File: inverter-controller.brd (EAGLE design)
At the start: 18.5 x 87.2 mm, 114 parts, among them IC1 STM32F334C8T6, IC2 SY7152ABC, IC3 LMV358MMX, IC4 LMV358MMX, J1 621006245821, J2 61300211121, X1 0289-9066**15EDGVC-3.81-02P-14, X2 0289-9066**15EDGVC-3.81-02P-14, X6 1365-16, Y1 NX2016SA-32M

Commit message: RS485 eklendi.
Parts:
- added C49, C50: 1019-3166**CAP 0603 CER 100nF 16V %10 X7R (AbC), rcl:C0603
- added C51, C53: 1019-3168","CAP 0805 CER 2.2uF 16V %10 X7R (AbC), rcl:C0805
- added C52: 0019-3020","CAP TH CER 470pF 3kV Y5P %10 85C F=7.5 D=8.5, rcl:C050-055X075
- added C60, C61: 1200920378**CAP 0603 CER 100p 50V%5 NP0, rcl:C0603
- added C66: NC, rcl:C0603
- added D10: 1119-3034_ESD Protection Diode for CANBUS NXP PESD2CAN SOT23, diode:SOT23
- added IC10: ISO3082, enko:ISO3082
- added L1: 1319-4025","INDUCTOR SMD 0805 4.7uH 500mA CL2012C-4R7M Core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, rcl:R0805
- added L6: 1319-4002_ACM2012 SMD Common Mode Filter, enko:ACM2012-900--2P-T002
- added LED4: 1209-0004**LED GREEN CLEAR THIN 0805 SMD, led:CHIP-LED0805
- added Q17: 1039-2335","DC-DC Converter 5V to 5V 1W RFMM-0505S, enko:RFMM-0505S
- added R41: 1029-2232**RES 0603 120R %1, rcl:R0603
- added R48: 1409-0025**RES 0603 470R %5 1/16W, rcl:R0603
- added R65, R66, R69: 1029-2003**RES 0603 10R %1, rcl:R0603
- added TP11, TP4, TP5, TP6, TP7, TP8: PTR1TP18R, testpad:TP18R
- added X3: 0289-9068**15EDGVC-3.81-03P-14, con-phoenix-381_l:MCV3
- moved X2 12.4 mm to (4.24, 12.8), turned to 90 degrees
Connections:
- new net +5V: C51.1, L1.1
- new net 485A_PORT: D10.1, R41.1, R69.1, X3.2
- new net 485B_PORT: D10.2, R41.2, R66.2, X3.1
- new net 485G_PORT1: C66.1, R65.2, X3.3
- new net N$24: LED4.A, R48.2
- new net N$41: C61.1, IC10.12, L6.2, TP8.TP
- new net N$42: L6.4, R66.1
- new net N$57: L6.3, R69.2
- new net N$73: C60.2, IC10.13, L6.1, TP7.TP
- new net N$80: C52.1, L1.2, Q17.1
- new net RS485_DIR: IC1.39, IC10.4, IC10.5, TP5.TP
- new net RS485_ISO_5V: C50.2, C52.2, C53.1, IC10.16, Q17.7
- new net RS485_ISO_GND: C50.1, C53.2, C60.1, C61.2, C66.2, D10.3, IC10.10, IC10.15, IC10.9, Q17.5, R65.1
- new net RS485_LED: IC1.40, LED4.C, TP11.TP
- new net RS485_RX: IC1.22, IC10.3, TP4.TP
- new net RS485_TX: IC1.21, IC10.6, TP6.TP
- net +3V3: now also C49.2, IC10.1, R48.1
- net GND: now also C49.1, C51.2, IC10.2, IC10.7, IC10.8, Q17.2

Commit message: RS485 DC-DC besleme gerilimi 3V yapildi.
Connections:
- removed net +5V: C51.1, L1.1
- net +3V3: now also C51.1, L1.1
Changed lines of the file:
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@@
 <contactref element="IC10" pad="1"/>
 <contactref element="R48" pad="1"/>
+<contactref element="C51" pad="1"/>
+<contactref element="L1" pad="1"/>
 <wire x1="-132.7238" y1="-366.64" x2="-132.7238" y2="-371.63" width="0" layer="19" extent="1-1"/>
 <wire x1="-132.7238" y1="-376.62" x2="-132.7238" y2="-371.63" width="0" layer="19" extent="1-1"/>
@@
 <wire x1="-27.91" y1="111.76" x2="5.172" y2="58.76" width="0" layer="19" extent="1-16"/>
 <wire x1="-96.445" y1="-593.1" x2="-132.7238" y2="-376.62" width="0" layer="19" extent="1-1"/>
-<wire x1="-144.85" y1="-690.5" x2="-96.445" y2="-593.1" width="0" layer="19" extent="1-1"/>
+<wire x1="-144.55" y1="-671.5" x2="-96.445" y2="-593.1" width="0" layer="19" extent="1-1"/>
+<wire x1="-144.55" y1="-684.5" x2="-144.55" y2="-671.5" width="0" layer="19" extent="1-1"/>
+<wire x1="-144.85" y1="-690.5" x2="-144.55" y2="-684.5" width="0" layer="19" extent="1-1"/>
 <wire x1="-116.15" y1="-701.5" x2="-144.85" y2="-690.5" width="0" layer="19" extent="1-1"/>
 </signal>
@@
 <wire x1="-124.9862" y1="-152.14" x2="-131.81" y2="-166.08" width="0" layer="19" extent="1-1"/>
 </signal>
-<signal name="+5V">
-<contactref element="C51" pad="1"/>
-<contactref element="L1" pad="1"/>
-<wire x1="-144.55" y1="-671.5" x2="-144.55" y2="-684.5" width="0" layer="19" extent="1-1"/>
-</signal>
 <signal name="485G_PORT1">

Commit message: Programlama soketi baglantilari duzeltildi.
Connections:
- net FAN2_EN renamed SWDIO
- removed net RELAY_EN: J1.2
- removed net SPI1_SCK: J1.6
- new net SWCLK: IC1.37, J1.2
- new net SWO: IC1.39, J1.6
- net RS485_DIR: now also IC1.41; no longer IC1.39
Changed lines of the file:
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@@
 <wire x1="-80.54" y1="106.68" x2="-74.19" y2="106.68" width="0" layer="19" extent="1-1"/>
-</signal>
-<signal name="SPI1_SCK">
-<contactref element="J1" pad="6"/>
 </signal>
 <signal name="NRST">
@@
 <wire x1="-131.1362" y1="-430.12" x2="-136.76" y2="-430.53" width="0" layer="19" extent="1-1"/>
 </signal>
-<signal name="FAN2_EN">
-<contactref element="IC1" pad="34"/>
-<contactref element="J1" pad="4"/>
-<wire x1="13.648" y1="55.76" x2="13.83" y2="84.16" width="0" layer="19" extent="1-16"/>
-</signal>
-<signal name="RELAY_EN">
-<contactref element="J1" pad="2"/>
-</signal>
 <signal name="N$35">
 <contactref element="LED8" pad="A"/>
@@
 <contactref element="IC10" pad="5"/>
 <contactref element="TP5" pad="TP"/>
-<contactref element="IC1" pad="39"/>
+<contactref element="IC1" pad="41"/>
 <wire x1="-91.365" y1="-593.1" x2="-92.635" y2="-593.1" width="0" layer="19" extent="1-1"/>
 <wire x1="-79" y1="-718" x2="-91.365" y2="-593.1" width="0" layer="19" extent="1-1"/>
-<wire x1="11.16" y1="53.272" x2="-91.365" y2="-593.1" width="0" layer="19" extent="1-16"/>
+<wire x1="10.16" y1="53.272" x2="-91.365" y2="-593.1" width="0" layer="19" extent="1-16"/>
 </signal>
 <signal name="RS485_TX">
@@
 <wire x1="11.16" y1="61.748" x2="-93.905" y2="-593.1" width="0" layer="19" extent="1-16"/>
 </signal>
+<signal name="SWO">
+<contactref element="IC1" pad="39"/>
+<contactref element="J1" pad="6"/>
+<wire x1="11.16" y1="53.272" x2="15.83" y2="84.16" width="0" layer="19" extent="1-16"/>
+</signal>
+<signal name="SWDIO">
+<contactref element="IC1" pad="34"/>
+<contactref element="J1" pad="4"/>
+<wire x1="13.648" y1="55.76" x2="13.83" y2="84.16" width="0" layer="19" extent="1-16"/>
+</signal>
+<signal name="SWCLK">
+<contactref element="IC1" pad="37"/>
+<contactref element="J1" pad="2"/>
+<wire x1="12.16" y1="53.272" x2="11.83" y2="84.16" width="0" layer="19" extent="1-16"/>
+</signal>
 </signals>

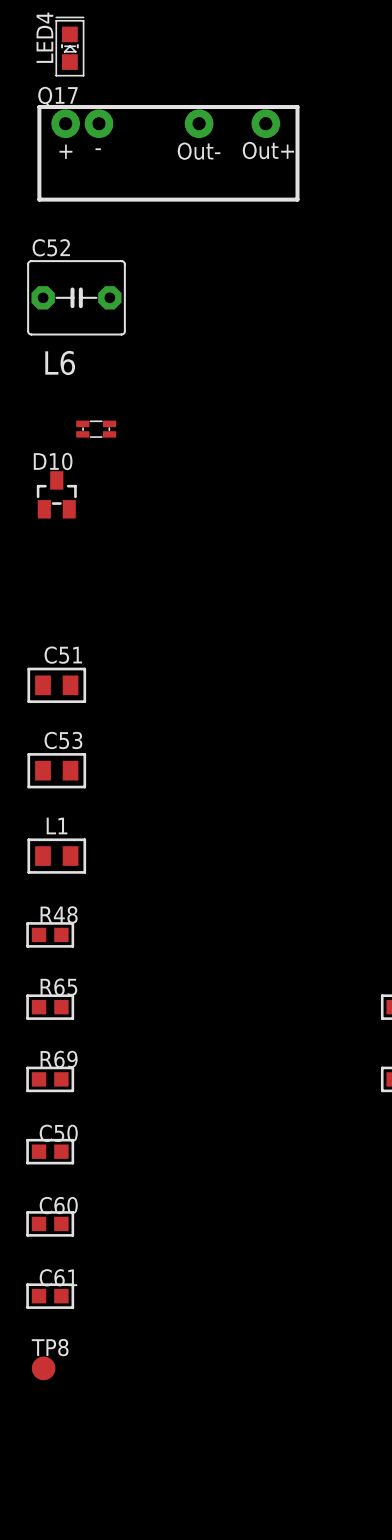
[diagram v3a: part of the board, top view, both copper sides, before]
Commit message: RS485 DC-DC paketi degistirildi.
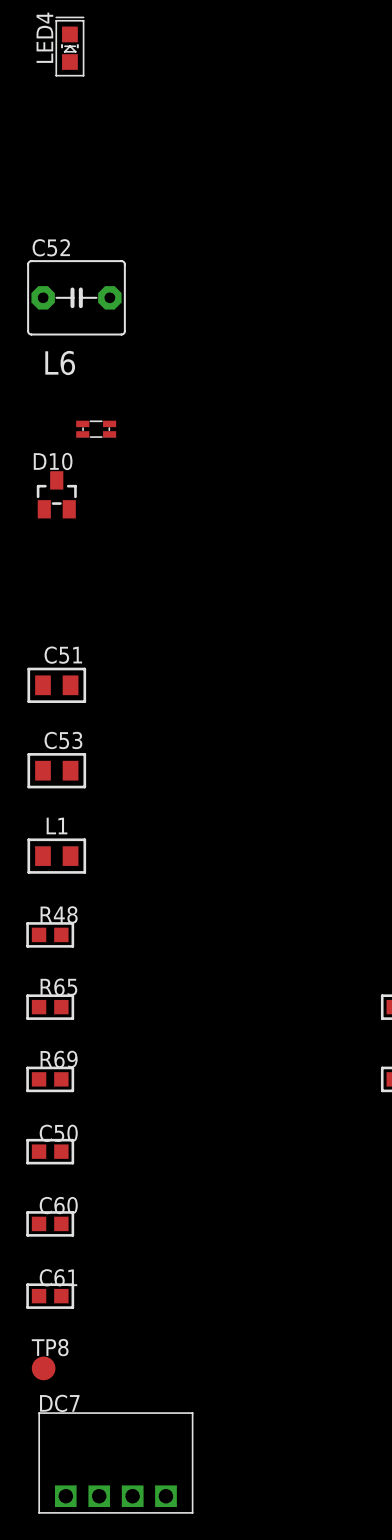
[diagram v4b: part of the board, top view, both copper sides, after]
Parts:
- removed Q17: 1039-2335","DC-DC Converter 5V to 5V 1W RFMM-0505S, enko:RFMM-0505S
- added DC7: RI-0512S/P_DC_DC_5V_12V, my_parts1:RI-0512S/P_DC_DC_5V_12V
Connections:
- removed net RELAY3: IC1.26
- removed net USART1_DIR: IC1.2
- net GND: now also DC7.1-IN; no longer Q17.2
- net N$80: now also DC7.2+IN; no longer Q17.1
- net RS485_ISO_5V: now also DC7.4+VOU; no longer Q17.7
- net RS485_ISO_GND: now also DC7.3-VOUT; no longer Q17.5
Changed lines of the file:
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@@
 <attribute name="VALUE" x="-138.85" y="-594.834" size="1.778" layer="27" ratio="10"/>
-</element>
-<element name="Q17" library="enko" package="RFMM-0505S" value="1039-2335&quot;,&quot;DC-DC Converter 5V to 5V 1W RFMM-0505S" x="-135" y="-631" smashed="yes">
-<attribute name="NAME" x="-145" y="-627.23" size="1.27" layer="25"/>
-<attribute name="VALUE" x="-145.12" y="-636.02" size="1.27" layer="27"/>
 </element>
 <element name="C51" library="rcl" package="C0805" value="1019-3168&quot;,&quot;CAP 0805 CER 2.2uF 16V %10 X7R (AbC)" x="-143.5" y="-671.5" smashed="yes">
@@
 <attribute name="TP_SIGNAL_NAME" value="" x="-89" y="-720.54" size="1" layer="37"/>
 <attribute name="VALUE" x="-89.762" y="-718.889" size="0.0254" layer="27"/>
+</element>
+<element name="DC7" library="my_parts1" package="RI-0512S/P_DC_DC_5V_12V" value="RI-0512S/P_DC_DC_5V_12V" x="-139" y="-734.5" smashed="yes">
+<attribute name="NAME" x="-144.93" y="-726.8" size="1.27" layer="25"/>
+<attribute name="VALUE" x="-145.07" y="-735.88" size="1.27" layer="27"/>
 </element>
 </elements>
@@
 <wire x1="-68.58" y1="53.34" x2="8.66" y2="53.272" width="0" layer="19" extent="16-16"/>
 <wire x1="-131.1362" y1="-184.29" x2="-68.58" y2="53.34" width="0" layer="19" extent="1-1"/>
-</signal>
-<signal name="USART1_DIR">
-<contactref element="IC1" pad="2"/>
 </signal>
 <signal name="GND">
@@
 <contactref element="IC10" pad="8"/>
 <contactref element="C51" pad="2"/>
-<contactref element="Q17" pad="2"/>
+<contactref element="DC7" pad="1-IN"/>
 <wire x1="-131.1362" y1="-371.63" x2="-131.1362" y2="-376.62" width="0" layer="19" extent="1-1"/>
 <wire x1="-131.1362" y1="-366.64" x2="-131.1362" y2="-371.63" width="0" layer="19" extent="1-1"/>
@@
 <wire x1="-145.0238" y1="-577.86" x2="-145.0238" y2="-570.66" width="0" layer="19" extent="1-1"/>
 <wire x1="-145.0238" y1="-581.46" x2="-145.0238" y2="-577.86" width="0" layer="19" extent="1-1"/>
-<wire x1="-140.285" y1="-628.745" x2="-145.0238" y2="-581.46" width="0" layer="19" extent="1-1"/>
-<wire x1="-142.45" y1="-671.5" x2="-140.285" y2="-628.745" width="0" layer="19" extent="1-1"/>
-<wire x1="-117.85" y1="-701.5" x2="-142.45" y2="-671.5" width="0" layer="19" extent="1-1"/>
 <wire x1="-95.175" y1="-593.1" x2="-145.0238" y2="-581.46" width="0" layer="19" extent="1-1"/>
 <wire x1="-88.825" y1="-593.1" x2="-95.175" y2="-593.1" width="0" layer="19" extent="1-1"/>
 <wire x1="-87.555" y1="-593.1" x2="-88.825" y2="-593.1" width="0" layer="19" extent="1-1"/>
+<wire x1="-142.45" y1="-671.5" x2="-145.0238" y2="-581.46" width="0" layer="19" extent="1-1"/>
+<wire x1="-117.85" y1="-701.5" x2="-142.45" y2="-671.5" width="0" layer="19" extent="1-1"/>
+<wire x1="-142.81" y1="-733.23" x2="-117.85" y2="-701.5" width="0" layer="19" extent="1-1"/>
 <wire x1="-24.426" y1="28.367" x2="-118.11" y2="-40.87" width="0" layer="19" extent="1-1"/>
 <wire x1="-15.536" y1="28.367" x2="-24.426" y2="28.367" width="0" layer="19" extent="1-1"/>
@@
 <wire x1="-76.94" y1="106.68" x2="-131.1362" y2="-344.47" width="0" layer="19" extent="1-1"/>
 </signal>
-<signal name="RELAY3">
-<contactref element="IC1" pad="26"/>
-</signal>
 <signal name="LED2">
 <contactref element="IC1" pad="4"/>
@@
 </signal>
 <signal name="N$80">
-<contactref element="Q17" pad="1"/>
 <contactref element="C52" pad="1"/>
 <contactref element="L1" pad="2"/>
+<contactref element="DC7" pad="2+IN"/>
+<wire x1="-142.45" y1="-684.5" x2="-140.27" y2="-733.23" width="0" layer="19" extent="1-1"/>
+<wire x1="-144.54" y1="-642" x2="-142.45" y2="-684.5" width="0" layer="19" extent="1-1"/>
 </signal>
 <signal name="RS485_ISO_5V">
-<contactref element="Q17" pad="7"/>
 <contactref element="C53" pad="1"/>
 <contactref element="C52" pad="2"/>
 <contactref element="C50" pad="2"/>
 <contactref element="IC10" pad="16"/>
+<contactref element="DC7" pad="4+VOU"/>
+<wire x1="-139.46" y1="-642" x2="-96.445" y2="-583.9" width="0" layer="19" extent="1-1"/>
+<wire x1="-144.55" y1="-678" x2="-139.46" y2="-642" width="0" layer="19" extent="1-1"/>
+<wire x1="-143.15" y1="-707" x2="-144.55" y2="-678" width="0" layer="19" extent="1-1"/>
+<wire x1="-135.19" y1="-733.23" x2="-143.15" y2="-707" width="0" layer="19" extent="1-1"/>
 </signal>
 <signal name="RS485_ISO_GND">
-<contactref element="Q17" pad="5"/>
 <contactref element="C53" pad="2"/>
 <contactref element="IC10" pad="10"/>
@@
 <contactref element="R65" pad="1"/>
 <contactref element="C66" pad="2"/>
-<wire x1="-143.5" y1="-655.9" x2="-132.665" y2="-628.745" width="0" layer="19" extent="1-1"/>
+<contactref element="DC7" pad="3-VOUT"/>
+<wire x1="-88.825" y1="-583.9" x2="-95.175" y2="-583.9" width="0" layer="19" extent="1-1"/>
+<wire x1="-87.555" y1="-583.9" x2="-88.825" y2="-583.9" width="0" layer="19" extent="1-1"/>
+<wire x1="-143.5" y1="-655.9" x2="-95.175" y2="-583.9" width="0" layer="19" extent="1-1"/>
 <wire x1="-142.45" y1="-678" x2="-143.5" y2="-655.9" width="0" layer="19" extent="1-1"/>
 <wire x1="-144.85" y1="-696" x2="-142.45" y2="-678" width="0" layer="19" extent="1-1"/>
@@
 <wire x1="-144.85" y1="-712.5" x2="-144.85" y2="-707" width="0" layer="19" extent="1-1"/>
 <wire x1="-143.15" y1="-718" x2="-144.85" y2="-712.5" width="0" layer="19" extent="1-1"/>
-<wire x1="-92.65" y1="-718" x2="-143.15" y2="-718" width="0" layer="19" extent="1-1"/>
-<wire x1="-95.175" y1="-583.9" x2="-132.665" y2="-628.745" width="0" layer="19" extent="1-1"/>
-<wire x1="-88.825" y1="-583.9" x2="-95.175" y2="-583.9" width="0" layer="19" extent="1-1"/>
-<wire x1="-87.555" y1="-583.9" x2="-88.825" y2="-583.9" width="0" layer="19" extent="1-1"/>
+<wire x1="-137.73" y1="-733.23" x2="-143.15" y2="-718" width="0" layer="19" extent="1-1"/>
+<wire x1="-92.65" y1="-718" x2="-137.73" y2="-733.23" width="0" layer="19" extent="1-1"/>
 </signal>
 <signal name="N$41">

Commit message: Fan ve NTC soketleri SMD-Pad kutuphanesi ile degistirildi.
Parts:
- removed X1, X2: 0289-9066**15EDGVC-3.81-02P-14, con-phoenix-381_l:MCV2
- added J3, J4: CONNECTOR-SMD-2PIN, Andromeda:CONNECTOR-SMD-2PIN
- moved X3 619.8 mm to (4.50, 15.0), turned to 90 degrees
- moved IC1 1.00 mm to (9.41, 58.5)
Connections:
- net +3V3: now also J3.1; no longer X2.1
- net N$10: now also J4.2; no longer X1.2
- net N$34: now also J4.1; no longer X1.1
- net NTC1: now also J3.2; no longer X2.2

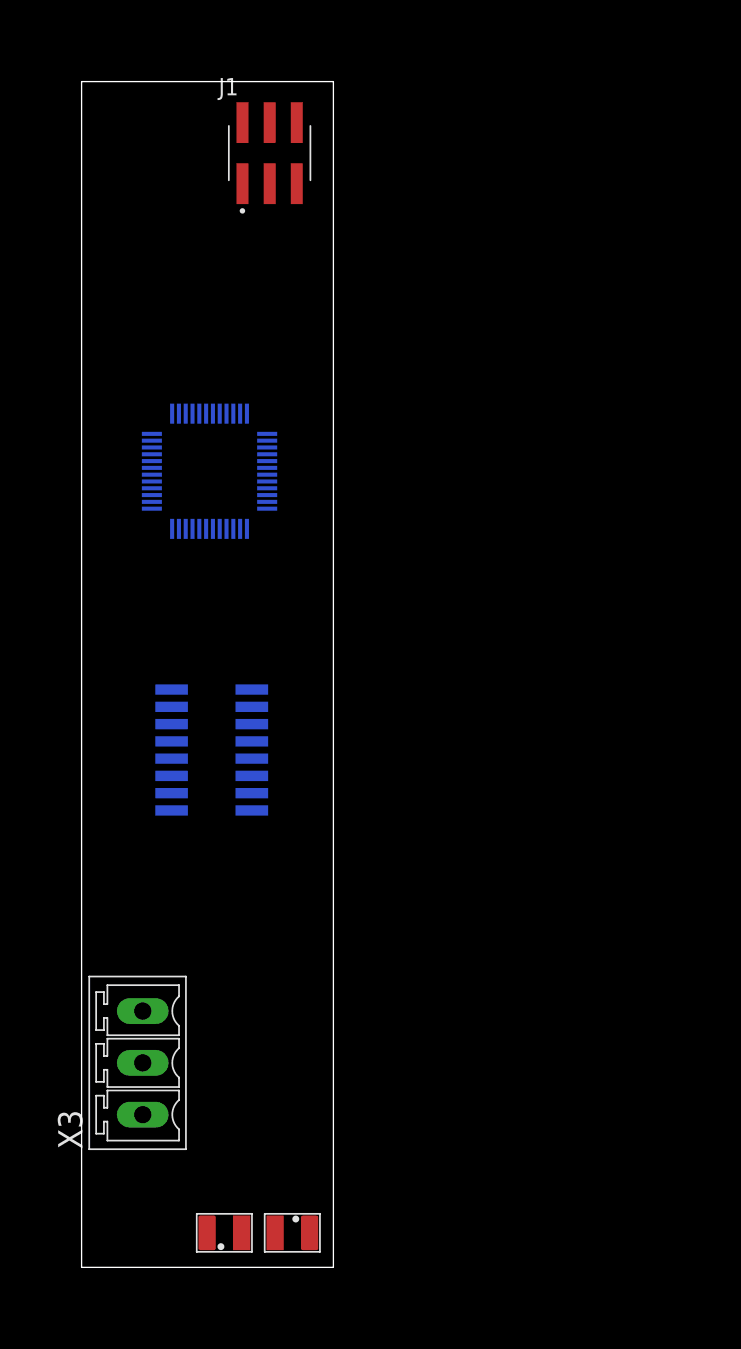
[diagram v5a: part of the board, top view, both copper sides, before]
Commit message: Board icin maksimum genisleme alani cizildi.
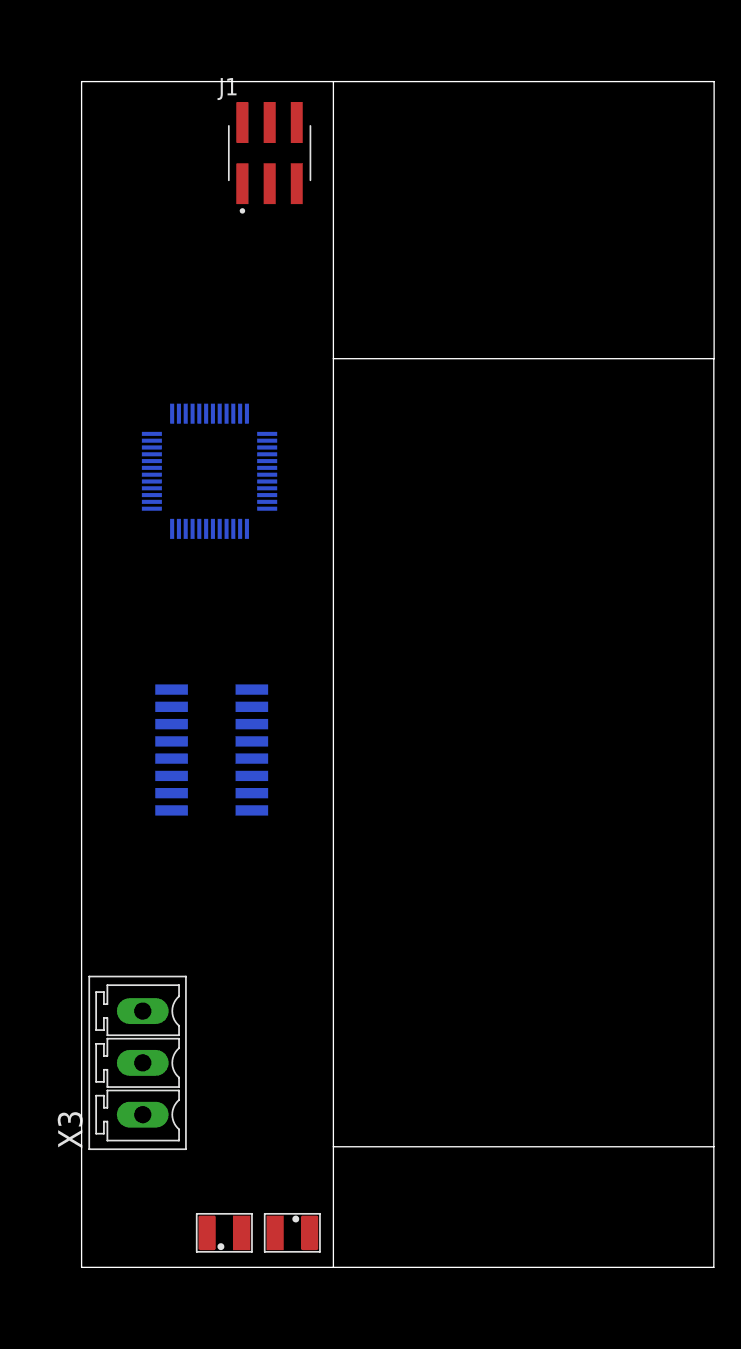
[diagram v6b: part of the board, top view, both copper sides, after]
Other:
- board size 18.5 x 87.2 mm -> 46.5 x 87.2 mm
